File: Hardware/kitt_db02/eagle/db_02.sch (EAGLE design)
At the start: 30 parts, among them J1 CON_HEADER_1X08-SMD, U1 MCP23017ML

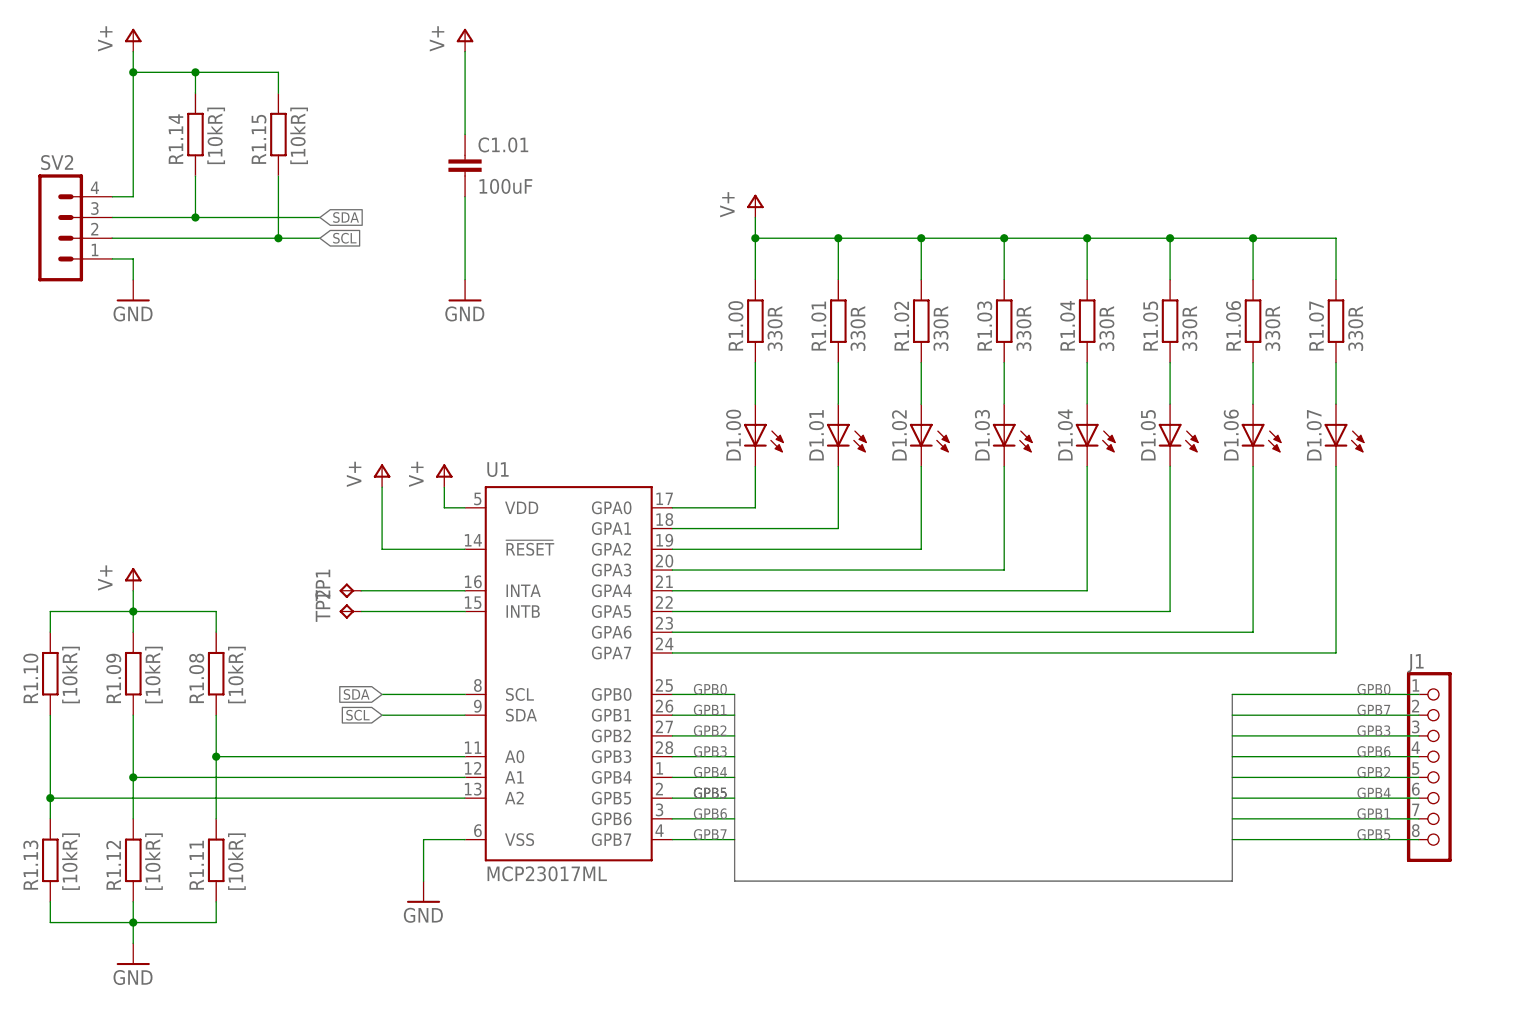
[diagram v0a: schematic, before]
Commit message: finished bonus board
it's a simple port expander via I2C,
plus it doubles as a neat bar indicator and is as wide as the cart itself.
why indicators? indicates directly the speed and brake-level visually.
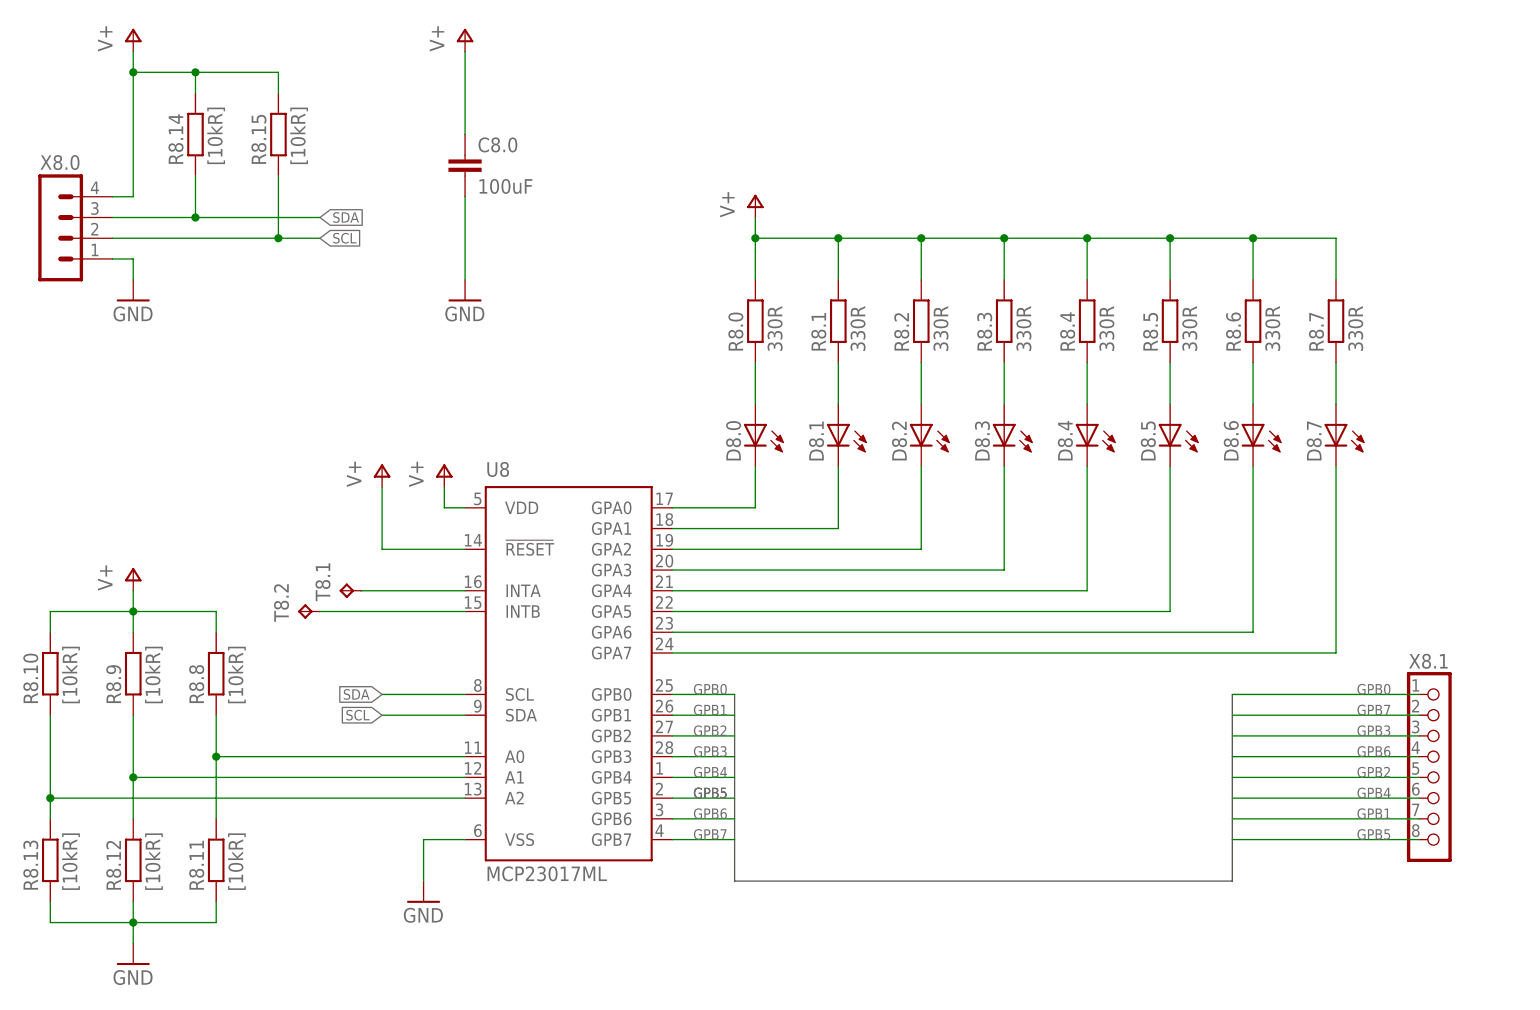
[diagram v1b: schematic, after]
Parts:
- removed TP1, TP2: TPTP16R, testpad:TPTP16R
- added T8.1, T8.2: TPTP09SQ, testpad:TPTP09SQ
- renumbered C1.01 to C8.0, D1.00 to D8.0, D1.01 to D8.1, D1.02 to D8.2, D1.03 to D8.3, D1.04 to D8.4, D1.05 to D8.5, D1.06 to D8.6, D1.07 to D8.7, J1 to X8.1, R1.00 to R8.0, R1.01 to R8.1, R1.02 to R8.2, R1.03 to R8.3, R1.04 to R8.4, R1.05 to R8.5, R1.06 to R8.6, R1.07 to R8.7, R1.08 to R8.8, R1.09 to R8.9, R1.10 to R8.10, R1.11 to R8.11, R1.12 to R8.12, R1.13 to R8.13, R1.14 to R8.14, R1.15 to R8.15, SV2 to X8.0, U1 to U8
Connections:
- net N$23: now also T8.1.TP; no longer TP1.TP
- net N$24: now also T8.2.TP; no longer TP2.TP

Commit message: snapshot of db02 board layout -> expanded gpio header to include gnd and supply -> tweaked routing -> added pours, also moved some stiches
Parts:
- removed X8.1: CON_HEADER_1X08-SMD, dp_devices:CON_HEADER_1X08-SMD
- added X1: CON_HEADER_1X10, kitt.con:CON_HEADER_1X10
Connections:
- net GND: now also X1.P$9
- net GPB0: now also X1.P$1; no longer X8.1.1
- net GPB1: now also X1.P$7; no longer X8.1.7
- net GPB2: now also X1.P$5; no longer X8.1.5
- net GPB3: now also X1.P$3; no longer X8.1.3
- net GPB4: now also X1.P$6; no longer X8.1.6
- net GPB5: now also X1.P$8; no longer X8.1.8
- net GPB6: now also X1.P$4; no longer X8.1.4
- net GPB7: now also X1.P$2; no longer X8.1.2
- net V+: now also X1.P$10
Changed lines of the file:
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@@
 <setting verticaltext="up"/>
 </settings>
-<grid distance="0.1" unitdist="inch" unit="inch" style="lines" multiple="1" display="no" altdistance="0.01" altunitdist="inch" altunit="inch"/>
+<grid distance="0.05" unitdist="inch" unit="inch" style="lines" multiple="1" display="no" altdistance="0.01" altunitdist="inch" altunit="inch"/>
 <layers>
 <layer number="1" name="Top" color="4" fill="1" visible="no" active="no"/>
@@
 <part name="GND3" library="supply1" deviceset="GND" device=""/>
 <part name="P+5" library="supply1" deviceset="V+" device=""/>
-<part name="X8.1" library="dp_devices" deviceset="CON_HEADER_1X08" device="-SMD"/>
 <part name="T8.1" library="testpad" deviceset="TP" device="TP09SQ" value="TPTP09SQ"/>
 <part name="T8.2" library="testpad" deviceset="TP" device="TP09SQ" value="TPTP09SQ"/>
@@
 <part name="GND4" library="supply1" deviceset="GND" device=""/>
 <part name="P+6" library="supply1" deviceset="V+" device=""/>
+<part name="X1" library="kitt.con" deviceset="CON_HEADER_1X10" device=""/>
+<part name="P+7" library="supply1" deviceset="V+" device=""/>
+<part name="GND5" library="supply1" deviceset="GND" device=""/>
 </parts>
 <sheets>
@@
 <instance part="GND3" gate="1" x="-25.4" y="0"/>
 <instance part="P+5" gate="1" x="5.08" y="60.96"/>
-<instance part="X8.1" gate="J" x="132.08" y="25.4"/>
 <instance part="T8.1" gate="G$1" x="0" y="45.72" rot="R90"/>
 <instance part="T8.2" gate="G$1" x="-5.08" y="43.18" rot="R90"/>
@@
 <instance part="GND4" gate="1" x="15.24" y="81.28"/>
 <instance part="P+6" gate="1" x="15.24" y="114.3"/>
+<instance part="X1" gate="G$1" x="138.43" y="25.4"/>
+<instance part="P+7" gate="1" x="125.73" y="10.16" rot="R90"/>
+<instance part="GND5" gate="1" x="129.54" y="0"/>
 </instances>
 <busses>
@@
 <wire x1="15.24" y1="111.76" x2="15.24" y2="101.6" width="0.1524" layer="91"/>
 </segment>
+<segment>
+<pinref part="P+7" gate="1" pin="V+"/>
+<pinref part="X1" gate="G$1" pin="P$10"/>
+<wire x1="128.27" y1="10.16" x2="132.08" y2="10.16" width="0.1524" layer="91"/>
+</segment>
 </net>
 <net name="GND" class="0">
@@
 <wire x1="15.24" y1="93.98" x2="15.24" y2="83.82" width="0.1524" layer="91"/>
 </segment>
+<segment>
+<pinref part="X1" gate="G$1" pin="P$9"/>
+<pinref part="GND5" gate="1" pin="GND"/>
+<wire x1="132.08" y1="12.7" x2="129.54" y2="12.7" width="0.1524" layer="91"/>
+<wire x1="129.54" y1="12.7" x2="129.54" y2="2.54" width="0.1524" layer="91"/>
+</segment>
 </net>
 <net name="SDA" class="0">
@@
 </segment>
 <segment>
-<pinref part="X8.1" gate="J" pin="1"/>
 <wire x1="132.08" y1="33.02" x2="109.22" y2="33.02" width="0.1524" layer="91"/>
 <label x="124.46" y="33.02" size="1.27" layer="95"/>
+<pinref part="X1" gate="G$1" pin="P$1"/>
 </segment>
 </net>
@@
 </segment>
 <segment>
-<pinref part="X8.1" gate="J" pin="7"/>
 <wire x1="109.22" y1="17.78" x2="132.08" y2="17.78" width="0.1524" layer="91"/>
 <label x="124.46" y="17.78" size="1.27" layer="95"/>
+<pinref part="X1" gate="G$1" pin="P$7"/>
 </segment>
 </net>
 <net name="GPB2" class="0">
 <segment>
-<pinref part="X8.1" gate="J" pin="5"/>
 <wire x1="109.22" y1="22.86" x2="132.08" y2="22.86" width="0.1524" layer="91"/>
 <label x="124.46" y="22.86" size="1.27" layer="95"/>
+<pinref part="X1" gate="G$1" pin="P$5"/>
 </segment>
 <segment>
@@
 </segment>
 <segment>
-<pinref part="X8.1" gate="J" pin="3"/>
 <wire x1="132.08" y1="27.94" x2="109.22" y2="27.94" width="0.1524" layer="91"/>
 <label x="124.46" y="27.94" size="1.27" layer="95"/>
+<pinref part="X1" gate="G$1" pin="P$3"/>
 </segment>
 </net>
@@
 </segment>
 <segment>
-<pinref part="X8.1" gate="J" pin="6"/>
 <wire x1="109.22" y1="20.32" x2="132.08" y2="20.32" width="0.1524" layer="91"/>
 <label x="124.46" y="20.32" size="1.27" layer="95"/>
+<pinref part="X1" gate="G$1" pin="P$6"/>
 </segment>
 </net>
@@
 </segment>
 <segment>
-<pinref part="X8.1" gate="J" pin="8"/>
 <wire x1="109.22" y1="15.24" x2="132.08" y2="15.24" width="0.1524" layer="91"/>
 <label x="124.46" y="15.24" size="1.27" layer="95"/>
+<pinref part="X1" gate="G$1" pin="P$8"/>
 </segment>
 </net>
 <net name="GPB6" class="0">
 <segment>
-<pinref part="X8.1" gate="J" pin="4"/>
 <wire x1="109.22" y1="25.4" x2="132.08" y2="25.4" width="0.1524" layer="91"/>
 <label x="124.46" y="25.4" size="1.27" layer="95"/>
+<pinref part="X1" gate="G$1" pin="P$4"/>
 </segment>
 <segment>
@@
 <net name="GPB7" class="0">
 <segment>
-<pinref part="X8.1" gate="J" pin="2"/>
 <wire x1="109.22" y1="30.48" x2="132.08" y2="30.48" width="0.1524" layer="91"/>
 <label x="124.46" y="30.48" size="1.27" layer="95"/>
-</segment>
-<segment>
+<pinref part="X1" gate="G$1" pin="P$2"/>
+</segment>
+<segment>
